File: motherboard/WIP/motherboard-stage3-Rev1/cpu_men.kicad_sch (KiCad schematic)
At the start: 28 parts, among them J1 HALT, J2 Write Enable, U2 74HC245, U3 MC6809, U4 74HC245, U5 28C64, U6 74HC245, U7 AS6C4008, U8 AS6C4008, Y1 12MHz

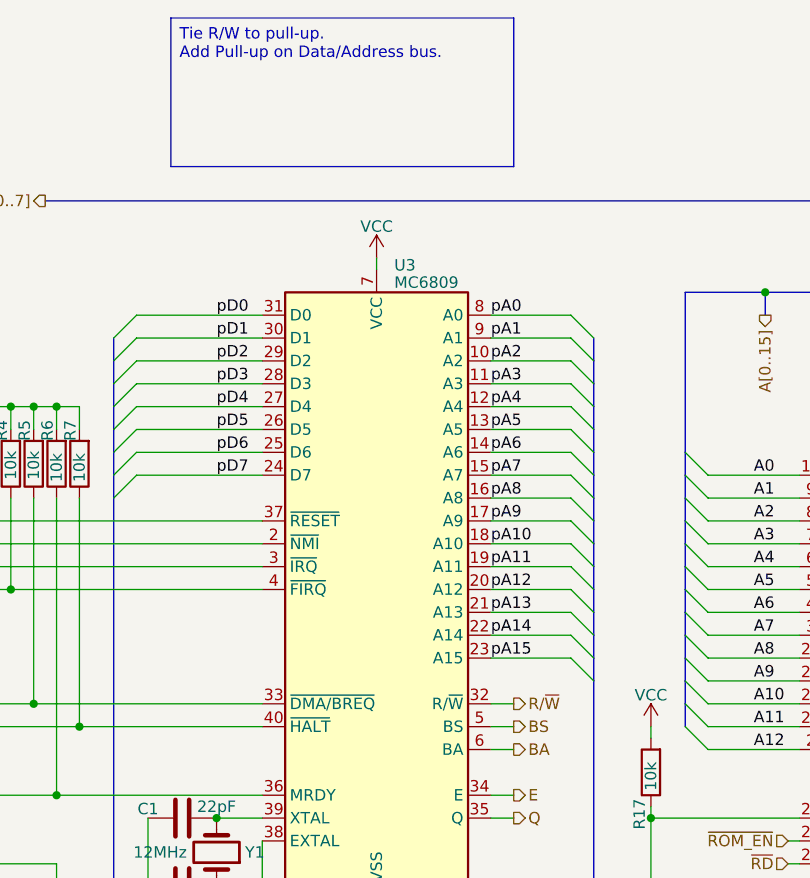
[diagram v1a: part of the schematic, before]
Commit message: Added Support for protected mode, routed R/W thru logic to amplify.
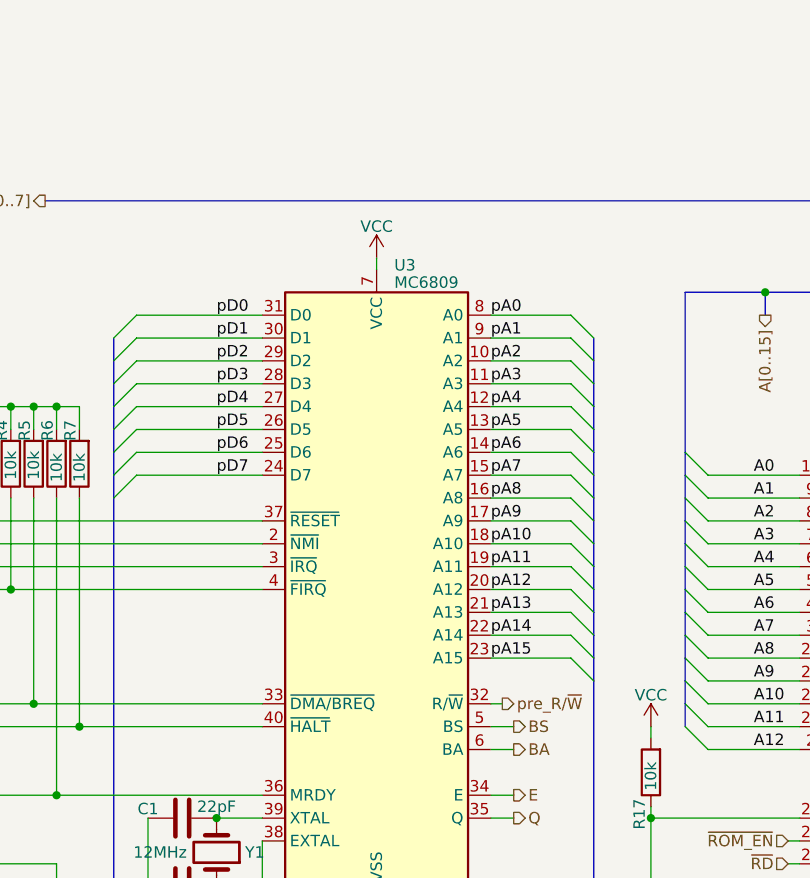
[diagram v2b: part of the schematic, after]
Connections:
- net R/~{W}: no longer U3.32 (R/~{W})
- new net pre_R/~{W}: U3.32 (R/~{W})
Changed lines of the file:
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@@
 		)
 	)
-	(text_box "Tie R/W to pull-up.\nAdd Pull-up on Data/Address bus."
-		(exclude_from_sim no)
-		(at 48.26 16.51 0)
-		(size 38.1 16.51)
-		(margins 0.9525 0.9525 0.9525 0.9525)
-		(stroke
-			(width 0)
-			(type default)
-		)
-		(fill
-			(type none)
-		)
-		(effects
-			(font
-				(size 1.27 1.27)
-			)
-			(justify left top)
-		)
-	)
 	(junction
 		(at 33.02 59.69)
@@
 	(wire
 		(pts
-			(xy 86.36 92.71) (xy 83.82 92.71)
+			(xy 85.09 92.71) (xy 83.82 92.71)
 		)
 		(stroke
@@
 		)
 	)
-	(hierarchical_label "R{slash}~{W}"
-		(shape output)
-		(at 86.36 92.71 0)
-		(effects
-			(font
-				(size 1.27 1.27)
-			)
-			(justify left)
-		)
-	)
 	(hierarchical_label "~{RAML_EN}"
 		(shape input)
@@
 		(effects
 			(font
+				(size 1.27 1.27)
+			)
+			(justify left)
+		)
+	)
+	(hierarchical_label "pre_R{slash}~{W}"
+		(shape output)
+		(at 85.09 92.71 0)
+		(effects
+			(font
